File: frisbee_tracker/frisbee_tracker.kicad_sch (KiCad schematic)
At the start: 18 parts, among them IC1 NRF54L05-QFAA-R7, J1 UJC-H-G-SMT-2-P6-TR, U1 AP2210N-3.3TRG1, U2 BQ24072RGTT, U3 BMI323

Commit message: Rough draft of schematic complete
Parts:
- added AE1: RFANT3216120A5T, ANT_RFANT3216120A5T_WAL, symbol RFANT3216120A5T:RFANT3216120A5T
- added C10, C11, C8, C9: 0.1 uF Ceramic, symbol Device:C
- added C12: 2.2 nF Ceramic, symbol Device:C
- added C13, C14: 2.2 uF Ceramic, symbol Device:C
- added C15: 10 nF Ceramic, symbol Device:C
- added C16: 3.9 pF Ceramic, symbol Device:C
- added C17, C18: 100nF Ceramic, symbol Device:C
- added C19: 100 nF Ceramic, symbol Device:C
- added C20: GJM0335C1E1R5WB01, symbol Device:C
- added C21: GJM0335C1E2R0WB01, symbol Device:C
- added C22: 0.3 pF Ceramic, symbol Device:C
- added C7: 10 uF Ceramic, symbol Device:C
- added D1, D2, D3, D4: 5991090147F, symbol Device:LED
- added FB1: BLM18KG121TN1D, symbol Device:FerriteBead
- added J2: FTSH-105-01-L-DV-K, digikey-footprints:PinHeader_2x5_P1.27_SMD, symbol dk_Rectangular-Connectors-Headers-Male-Pins:FTSH-105-01-L-DV-K
- added L1: 4.7 uH, symbol Device:L
- added L2: LQP03HQ2N7B02, symbol Device:L
- added L3, L4: LQP03HQ3N5B02, symbol Device:L
- added R10, R7, R8: 4.7 kOhm, symbol Device:R_US
- added R11, R12, R13, R14: 68 Ohm, symbol Device:R_US
- added R15, R16: 10 kOhm, symbol Device:R_US
- added R17: 1 MOhm, symbol Device:R_US
- added R6: 1 kOhm, symbol Device:R_US
- added R9: 1.3 kOhm, symbol Device:R_US
- added U4, U5, U6, U7: BSS138, SOT-23_3L_ONS, symbol BSS138:BSS138
- added Y1: 32 MHz, symbol Device:Crystal
- added Y2: 32.768 kHz, symbol Device:Crystal
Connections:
- net GND: now also IC1.32 (VSS_PA), IC1.44 (VSS), IC1.49 (EP), U3.1 (SDO), U3.6 (GNDIO), U3.7 (GND), C10.1, C11.1, C12.1, C13.1, C14.1, C15.1, C16.1, C17.2, C18.1, C19.1, C20.1, C21.2, C22.1, C7.1, C8.1, C9.1, J2.3, J2.5, R10.2, R17.1, U4.2 (S), U5.2 (S), U6.2 (S), U7.2 (S)
- net at U2.14 (TMR): now also R17.2
- net at C3.1, H1.1, U2.2 (BAT)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: now also R9.2
- net at U2.7 (~{PGOOD}): now also IC1.18 (P2.07/TRACEDATA[0]/SWO/SPI.DCX), R16.1
- net at U2.9 (~{CHG}): now also IC1.17 (P2.06/TRACECLK/SPI.SCK), R15.1
- net at C6.1, U1.2 (VOUT): now also IC1.10 (VDD_1), IC1.22 (VDD_2), IC1.36 (VDD_3), IC1.47 (VDD_4), IC1.48 (VDD_5), U3.12 (CSB), U3.5 (VDDIO), U3.8 (VDD), C10.2, C11.2, C17.1, C18.2, C7.2, C8.2, C9.2, J2.1, R11.2, R12.2, R13.2, R14.2, R15.2, R16.2, R7.1, R8.1
- net at U3.13 (SCX): now also IC1.12 (P2.01/SPI.SCK), R8.2
- net at U3.14 (SDX): now also IC1.11 (P2.00/SPI.DCX), R7.2
- net at U3.4 (INT1): now also IC1.23 (P0.00)
- net at U3.9 (INT2): now also IC1.24 (P0.01)
- net at IC1.1 (P1.00/XL1): now also Y2.2
- net at IC1.13 (P2.02/SPI.SDI/SDO): now also U4.1 (G)
- net at IC1.14 (P2.03): now also U5.1 (G)
- net at IC1.15 (P2.04/SPI.SDI/SDO): now also U6.1 (G)
- net at IC1.16 (P2.05/SPI.CS): now also U7.1 (G)
- net at IC1.2 (P1.01/XL2): now also Y2.1
- net at IC1.25 (SWDIO): now also J2.2
- net at IC1.26 (SWDCLK): now also J2.4
- net at IC1.30 (NRESET): now also C16.2, R6.1
- net at IC1.31 (ANT): now also L2.1
- net at IC1.33 (DECRF): now also IC1.43 (DECA), C12.2, C13.2, C15.2, FB1.2
- net at IC1.34 (XC1): now also Y1.2
- net at IC1.35 (XC2): now also Y1.1
- net at IC1.45 (DECD): now also C14.2, FB1.1, L1.2
- net at IC1.46 (DCC): now also L1.1
- net at IC1.9 (P1.08/CLK16M/TAMPC): now also C19.2, R10.1, R9.1
- new net: D4.2 (A), R14.1
- new net: D2.1 (K), U5.3 (D)
- new net: D2.2 (A), R12.1
- new net: D3.2 (A), R13.1
- new net: D3.1 (K), U6.3 (D)
- new net: D1.1 (K), U4.3 (D)
- new net: D1.2 (A), R11.1
- new net: C20.2, L2.2, L3.1
- new net: C21.1, L3.2, L4.1
- new net: J2.6, R6.2
- new net: D4.1 (K), U7.3 (D)
- new net: AE1.1, C22.2, L4.2
- no-connect marks 1 -> 23
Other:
- note added: "C21 MUST ONLY CONNECT TO BOTTOM LAYER GROUND"
- note added: "C21:"
- note added: "C22:"
- note added: "CONNECT PIN 32 ONLY TO PIN 49 (CENTER PAD)"
- note added: "L2:"
- note added: "L3:"
- note added: "L4:"
- note added: "PUSH-PULL INTERRUPT CONFIG"
- moved on the sheet: H1, H2, U3

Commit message: start of PCB design
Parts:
- AE1: footprint ANT_RFANT3216120A5T_WAL -> footprints:RFANT3216120A5T
- C1, C10, C11, C12, C13, C14, C15, C16, C17, C18, C19, C2, C22, C3, C4, C5, C6, C7, C8, C9: footprint (none) -> Capacitor_SMD:C_0603_1608Metric
- C20, C21: footprint (none) -> Capacitor_SMD:C_0201_0603Metric
- D1, D2, D3, D4: footprint (none) -> LED_SMD:LED_0603_1608Metric
- FB1: footprint (none) -> footprints:BLM18KG121TN1D
- H1, H2: footprint (none) -> Connector_PinHeader_1.27mm:PinHeader_1x01_P1.27mm_Vertical
- IC1: footprint (none) -> footprints:NRF54L05-QFAA-R7
- J1: footprint (none) -> footprints:UJC-H-G-SMT-2-P6-TR
- J2: footprint digikey-footprints:PinHeader_2x5_P1.27_SMD -> footprints:FTSH-105-01-L-DV-K
- L1: footprint (none) -> Inductor_SMD:L_0603_1608Metric
- L2: footprint (none) -> footprints:LQP03HQ2N7B02D
- L3, L4: footprint (none) -> footprints:LQP03HQ3N5B02D
- R1, R10, R11, R12, R13, R14, R15, R16, R17, R2, R3, R4, R5, R6, R7, R8, R9: footprint (none) -> Resistor_SMD:R_0603_1608Metric
- U1: footprint (none) -> footprints:AP2210N-3.3TRG1
- U2: footprint (none) -> footprints:BQ24072RGTT
- U3: footprint (none) -> footprints:BMI323
- U4, U5, U6, U7: footprint SOT-23_3L_ONS -> footprints:BSS138
- Y1: footprint (none) -> footprints:ECS-320-8-37B2-JTY-TR
- Y2: footprint (none) -> footprints:Q 0,032768-JTX210-7-20-T1-HMR-70K-LF
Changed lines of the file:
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@@
 			)
 		)
-		(property "Footprint" ""
+		(property "Footprint" "footprints:Q 0,032768-JTX210-7-20-T1-HMR-70K-LF"
 			(at 38.1 88.9 0)
 			(effects
@@
 			)
 		)
-		(property "Footprint" ""
+		(property "Footprint" "Capacitor_SMD:C_0603_1608Metric"
 			(at 120.3452 35.56 0)
 			(effects
@@
 			)
 		)
-		(property "Footprint" ""
+		(property "Footprint" "Capacitor_SMD:C_0603_1608Metric"
 			(at 241.3 101.9048 0)
 			(effects
@@
 			)
 		)
-		(property "Footprint" ""
+		(property "Footprint" "Capacitor_SMD:C_0603_1608Metric"
 			(at 73.66 58.1152 0)
 			(effects
@@
 			)
 		)
-		(property "Footprint" ""
+		(property "Footprint" "Resistor_SMD:R_0603_1608Metric"
 			(at 20.066 176.784 90)
 			(effects
@@
 			)
 		)
-		(property "Footprint" ""
+		(property "Footprint" "LED_SMD:LED_0603_1608Metric"
 			(at 35.56 168.91 0)
 			(effects
@@
 			)
 		)
-		(property "Footprint" ""
+		(property "Footprint" "Resistor_SMD:R_0603_1608Metric"
 			(at 27.686 176.784 90)
 			(effects
@@
 			)
 		)
-		(property "Footprint" ""
+		(property "Footprint" "LED_SMD:LED_0603_1608Metric"
 			(at 26.67 168.91 0)
 			(effects
@@
 			)
 		)
-		(property "Footprint" ""
+		(property "Footprint" "Capacitor_SMD:C_0603_1608Metric"
 			(at 100.6348 46.99 0)
 			(effects
@@
 			)
 		)
-		(property "Footprint" ""
+		(property "Footprint" "Capacitor_SMD:C_0603_1608Metric"
 			(at 25.0952 116.84 0)
 			(effects
@@
 			)
 		)
-		(property "Footprint" ""
+		(property "Footprint" "footprints:BQ24072RGTT"
 			(at 228.6 73.66 0)
 			(effects
@@
 			)
 		)
-		(property "Footprint" ""
+		(property "Footprint" "Resistor_SMD:R_0603_1608Metric"
 			(at 181.356 45.974 90)
 			(effects
@@
 			)
 		)
-		(property "Footprint" "SOT-23_3L_ONS"
+		(property "Footprint" "footprints:BSS138"
 			(at -1.27 151.13 0)
 			(effects
@@
 			)
 		)
-		(property "Footprint" ""
+		(property "Footprint" "Capacitor_SMD:C_0603_1608Metric"
 			(at 261.62 57.4548 0)
 			(effects
@@
 			)
 		)
-		(property "Footprint" ""
+		(property "Footprint" "Resistor_SMD:R_0603_1608Metric"
 			(at 45.466 176.784 90)
 			(effects
@@
 			)
 		)
-		(property "Footprint" ""
+		(property "Footprint" "Resistor_SMD:R_0603_1608Metric"
 			(at 260.604 80.264 90)
 			(effects
@@
 			)
 		)
-		(property "Footprint" ""
+		(property "Footprint" "Capacitor_SMD:C_0603_1608Metric"
 			(at 265.43 72.6948 0)
 			(effects
@@
 			)
 		)
-		(property "Footprint" ""
+		(property "Footprint" "Capacitor_SMD:C_0603_1608Metric"
 			(at 125.73 48.5648 0)
 			(effects
@@
 			)
 		)
-		(property "Footprint" ""
+		(property "Footprint" "Resistor_SMD:R_0603_1608Metric"
 			(at 175.514 102.616 90)
 			(effects
@@
 			)
 		)
-		(property "Footprint" ""
+		(property "Footprint" "Resistor_SMD:R_0603_1608Metric"
 			(at 186.436 49.784 90)
 			(effects
@@
 			)
 		)
-		(property "Footprint" ""
+		(property "Footprint" "Capacitor_SMD:C_0603_1608Metric"
 			(at 266.7 20.6248 0)
 			(effects
@@
 			)
 		)
-		(property "Footprint" ""
+		(property "Footprint" "Connector_PinHeader_1.27mm:PinHeader_1x01_P1.27mm_Vertical"
 			(at 266.7 43.18 0)
 			(effects
@@
 			)
 		)
-		(property "Footprint" "SOT-23_3L_ONS"
+		(property "Footprint" "footprints:BSS138"
 			(at -1.27 179.07 0)
 			(effects
@@
 			)
 		)
-		(property "Footprint" ""
+		(property "Footprint" "footprints:LQP03HQ3N5B02D"
 			(at 154.94 93.98 0)
 			(effects
@@
 			)
 		)
-		(property "Footprint" ""
+		(property "Footprint" "Resistor_SMD:R_0603_1608Metric"
 			(at 167.894 102.616 90)
 			(effects
@@
 			)
 		)
-		(property "Footprint" ""
+		(property "Footprint" "footprints:BMI323"
 			(at 201.93 130.81 0)
 			(effects
@@
 			)
 		)
-		(property "Footprint" ""
+		(property "Footprint" "Resistor_SMD:R_0603_1608Metric"
 			(at 272.034 26.924 90)
 			(effects
@@
 			)
 		)
-		(property "Footprint" ""
+		(property "Footprint" "footprints:BLM18KG121TN1D"
 			(at 88.9 48.768 90)
 			(effects
@@
 			)
 		)
-		(property "Footprint" ""
+		(property "Footprint" "Resistor_SMD:R_0603_1608Metric"
 			(at 147.574 110.744 90)
 			(effects
@@
 			)
 		)
-		(property "Footprint" ""
+		(property "Footprint" "Capacitor_SMD:C_0603_1608Metric"
 			(at 130.5052 101.6 0)
 			(effects
@@
 			)
 		)
-		(property "Footprint" ""
+		(property "Footprint" "Capacitor_SMD:C_0603_1608Metric"
 			(at 64.77 57.4548 0)
 			(effects
@@
 			)
 		)
-		(property "Footprint" "SOT-23_3L_ONS"
+		(property "Footprint" "footprints:BSS138"
 			(at -1.27 193.04 0)
 			(effects
@@
 			)
 		)
-		(property "Footprint" ""
+		(property "Footprint" "Resistor_SMD:R_0603_1608Metric"
 			(at 139.446 32.004 90)
 			(effects
@@
 			)
 		)
-		(property "Footprint" ""
+		(property "Footprint" "Capacitor_SMD:C_0603_1608Metric"
 			(at 205.74 159.0548 0)
 			(effects
@@
 			)
 		)
-		(property "Footprint" "SOT-23_3L_ONS"
+		(property "Footprint" "footprints:BSS138"
 			(at -1.27 165.1 0)
 			(effects
@@
 			)
 		)
-		(property "Footprint" ""
+		(property "Footprint" "Resistor_SMD:R_0603_1608Metric"
 			(at 207.264 77.724 90)
 			(effects
@@
 			)
 		)
-		(property "Footprint" ""
+		(property "Footprint" "Capacitor_SMD:C_0603_1608Metric"
 			(at 64.77 48.5648 0)
 			(effects
@@
 			)
 		)
-		(property "Footprint" ""
+		(property "Footprint" "Capacitor_SMD:C_0603_1608Metric"
 			(at 87.63 194.0052 0)
 			(effects
@@
 			)
 		)
-		(property "Footprint" ""
+		(property "Footprint" "Capacitor_SMD:C_0201_0603Metric"
 			(at 147.32 91.1352 0)
 			(effects
@@
 			)
 		)
-		(property "Footprint" ""
+		(property "Footprint" "Resistor_SMD:R_0603_1608Metric"
 			(at 250.444 62.484 90)
 			(effects
@@
 			)
 		)
-		(property "Footprint" ""
+		(property "Footprint" "Capacitor_SMD:C_0603_1608Metric"
 			(at 154.94 81.5848 0)
 			(effects
@@
 			)
 		)
-		(property "Footprint" ""
+		(property "Footprint" "footprints:UJC-H-G-SMT-2-P6-TR"
 			(at 182.88 29.21 0)
 			(effects
@@
 			)
 		)
-		(property "Footprint" ""
+		(property "Footprint" "Capacitor_SMD:C_0603_1608Metric"
 			(at 140.6652 101.6 0)
 			(effects
@@
 			)
 		)
-		(property "Footprint" "ANT_RFANT3216120A5T_WAL"
+		(property "Footprint" "footprints:RFANT3216120A5T"
 			(at 142.24 73.66 0)
 			(effects
@@
 			)
 		)
-		(property "Footprint" ""
+		(property "Footprint" "footprints:ECS-320-8-37B2-JTY-TR"
 			(at 116.84 93.98 0)
 			(effects
@@
 			)
 		)
-		(property "Footprint" ""
+		(property "Footprint" "LED_SMD:LED_0603_1608Metric"
 			(at 44.45 168.91 0)
 			(effects
@@
 			)
 		)
-		(property "Footprint" ""
+		(property "Footprint" "Capacitor_SMD:C_0201_0603Metric"
 			(at 147.6248 99.06 0)
 			(effects
@@
 			)
 		)
-		(property "Footprint" ""
+		(property "Footprint" "footprints:LQP03HQ3N5B02D"
 			(at 154.94 86.36 0)
 			(effects
@@
 			)
 		)
-		(property "Footprint" ""
+		(property "Footprint" "LED_SMD:LED_0603_1608Metric"
 			(at 19.05 168.91 0)
 			(effects
@@
 			)
 		)
-		(property "Footprint" ""
+		(property "Footprint" "footprints:NRF54L05-QFAA-R7"
 			(at 106.68 173.66 0)
 			(effects
@@
 			)
 		)
-		(property "Footprint" ""
+		(property "Footprint" "Capacitor_SMD:C_0603_1608Metric"
 			(at 104.14 16.8148 0)
 			(effects
@@
 			)
 		)
-		(property "Footprint" ""
+		(property "Footprint" "Capacitor_SMD:C_0603_1608Metric"
 			(at 111.76 68.8848 0)
 			(effects
@@
 			)
 		)
-		(property "Footprint" ""
+		(property "Footprint" "Resistor_SMD:R_0603_1608Metric"
 			(at 36.576 176.784 90)
 			(effects
@@
 			)
 		)
-		(property "Footprint" ""
+		(property "Footprint" "footprints:LQP03HQ2N7B02D"
 			(at 154.94 101.6 0)
 			(effects
@@
 			)
 		)
-		(property "Footprint" ""
+		(property "Footprint" "Resistor_SMD:R_0603_1608Metric"
 			(at 170.434 153.416 90)
 			(effects
@@
 			)
 		)
-		(property "Footprint" ""
+		(property "Footprint" "Capacitor_SMD:C_0603_1608Metric"
 			(at 241.3 159.0548 0)
 			(effects
@@
 			)
 		)
-		(property "Footprint" ""
+		(property "Footprint" "Inductor_SMD:L_0603_1608Metric"
 			(at 76.2 46.99 0)
 			(effects
@@
 			)
 		)
-		(property "Footprint" "digikey-footprints:PinHeader_2x5_P1.27_SMD"
+		(property "Footprint" "footprints:FTSH-105-01-L-DV-K"
 			(at 152.4 58.42 0)
 			(effects
@@
 			)
 		)
-		(property "Footprint" ""
+		(property "Footprint" "Connector_PinHeader_1.27mm:PinHeader_1x01_P1.27mm_Vertical"
 			(at 279.4 43.18 0)
 			(effects
@@
 			)
 		)
-		(property "Footprint" ""
+		(property "Footprint" "Resistor_SMD:R_0603_1608Metric"
 			(at 180.594 153.416 90)
 			(effects
@@
 			)
 		)
-		(property "Footprint" ""
+		(property "Footprint" "Resistor_SMD:R_0603_1608Metric"
 			(at 267.716 34.544 90)
 			(effects
@@
 			)
 		)
-		(property "Footprint" ""
+		(property "Footprint" "footprints:AP2210N-3.3TRG1"
 			(at 71.12 29.21 0)
 			(effects
@@
 			)
 		)
-		(property "Footprint" ""
+		(property "Footprint" "Capacitor_SMD:C_0603_1608Metric"
 			(at 136.1948 111.76 0)
 			(effects

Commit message: PCB design 90% complete
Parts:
- removed J2: FTSH-105-01-L-DV-K, footprints:FTSH-105-01-L-DV-K, symbol dk_Rectangular-Connectors-Headers-Male-Pins:FTSH-105-01-L-DV-K
- added J2: FTSH-103-01-L-D, footprints:FTSH-103-01-L-D, symbol FTSH-103-01-L-D:FTSH-103-01-L-D
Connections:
- net GND: now also J2.03, J2.05
- net at C10.2, C11.2, C17.1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: now also J2.01
- net at IC1.18 (P2.07/TRACEDATA[0]/SWO/SPI.DCX), R16.1: now also U2.9 (~{CHG}); no longer U2.7 (~{PGOOD})
- net at IC1.17 (P2.06/TRACECLK/SPI.SCK), R15.1: now also U2.7 (~{PGOOD}); no longer U2.9 (~{CHG})
- net at R6.2: now also J2.06
- net at IC1.25 (SWDIO): now also J2.02
- net at IC1.26 (SWDCLK): now also J2.04
- no-connect marks 23 -> 19

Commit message: Rough draft of PCB completed
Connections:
- net at C1.2, J1.SH1 (SHIELD), J1.SH2 (SHIELD__1)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: no longer J1.SH3 (SHIELD__2), J1.SH4 (SHIELD__3)
- no-connect marks 19 -> 21
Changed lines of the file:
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@@
+	)
+	(junction
+		(at 165.1 43.18)
+		(diameter 0)
+		(color 0 0 0 0)
 	)
 	(junction
@@
 	)
 	(junction
-		(at 162.56 41.91)
-		(diameter 0)
-		(color 0 0 0 0)
-	)
-	(junction
 		(at 111.76 49.53)
 		(diameter 0)
@@
 	)
 	(junction
+		(at 138.43 43.18)
+		(diameter 0)
+		(color 0 0 0 0)
+	)
+	(junction
 		(at 111.76 40.64)
 		(diameter 0)
@@
 	)
 	(junction
-		(at 138.43 41.91)
-		(diameter 0)
-		(color 0 0 0 0)
-	)
-	(junction
 		(at 181.61 160.02)
 		(diameter 0)
@@
 	)
 	(junction
-		(at 160.02 41.91)
-		(diameter 0)
-		(color 0 0 0 0)
-	)
-	(junction
 		(at 44.45 193.04)
 		(diameter 0)
@@
 	(junction
 		(at 266.7 27.94)
-		(diameter 0)
-		(color 0 0 0 0)
-	)
-	(junction
-		(at 165.1 41.91)
 		(diameter 0)
 		(color 0 0 0 0)
@@
 	)
 	(no_connect
+		(at 160.02 41.91)
+	)
+	(no_connect
 		(at 44.45 109.22)
 	)
@@
 	)
 	(no_connect
+		(at 162.56 41.91)
+	)
+	(no_connect
 		(at 44.45 111.76)
 	)
@@
 	(wire
 		(pts
+			(xy 167.64 43.18) (xy 167.64 41.91)
+		)
+		(stroke
+			(width 0)
+			(type default)
+		)
+	)
+	(wire
+		(pts
 			(xy 67.31 172.72) (xy 67.31 201.93)
 		)
@@
 	(wire
 		(pts
-			(xy 165.1 41.91) (xy 167.64 41.91)
+			(xy 165.1 43.18) (xy 167.64 43.18)
 		)
 		(stroke
@@
 	(wire
 		(pts
-			(xy 119.38 35.56) (xy 119.38 41.91)
+			(xy 119.38 35.56) (xy 119.38 43.18)
 		)
 		(stroke
@@
 	(wire
 		(pts
-			(xy 119.38 41.91) (xy 138.43 41.91)
+			(xy 119.38 43.18) (xy 138.43 43.18)
 		)
 		(stroke
@@
 	(wire
 		(pts
-			(xy 160.02 41.91) (xy 162.56 41.91)
-		)
-		(stroke
-			(width 0)
-			(type default)
-		)
-	)
-	(wire
-		(pts
 			(xy 246.38 133.35) (xy 242.57 133.35)
 		)
@@
 	(wire
 		(pts
+			(xy 165.1 41.91) (xy 165.1 43.18)
+		)
+		(stroke
+			(width 0)
+			(type default)
+		)
+	)
+	(wire
+		(pts
 			(xy 120.65 101.6) (xy 120.65 93.98)
 		)
@@
 	(wire
 		(pts
-			(xy 138.43 41.91) (xy 138.43 35.56)
-		)
-		(stroke
-			(width 0)
-			(type default)
-		)
-	)
-	(wire
-		(pts
 			(xy 246.38 17.78) (xy 111.76 17.78)
 		)
@@
 	(wire
 		(pts
-			(xy 162.56 41.91) (xy 165.1 41.91)
-		)
-		(stroke
-			(width 0)
-			(type default)
-		)
-	)
-	(wire
-		(pts
 			(xy 246.38 115.57) (xy 246.38 133.35)
 		)
@@
 	(wire
 		(pts
+			(xy 165.1 43.18) (xy 138.43 43.18)
+		)
+		(stroke
+			(width 0)
+			(type default)
+		)
+	)
+	(wire
+		(pts
 			(xy 69.85 204.47) (xy 69.85 172.72)
 		)
@@
 	(wire
 		(pts
+			(xy 138.43 35.56) (xy 138.43 43.18)
+		)
+		(stroke
+			(width 0)
+			(type default)
+		)
+	)
+	(wire
+		(pts
 			(xy 111.76 44.45) (xy 111.76 49.53)
 		)
@@
 		)
 		(stroke
-			(width 0)
-			(type default)
-		)
-	)
-	(wire
-		(pts
-			(xy 138.43 41.91) (xy 160.02 41.91)
-		)
-		(stroke

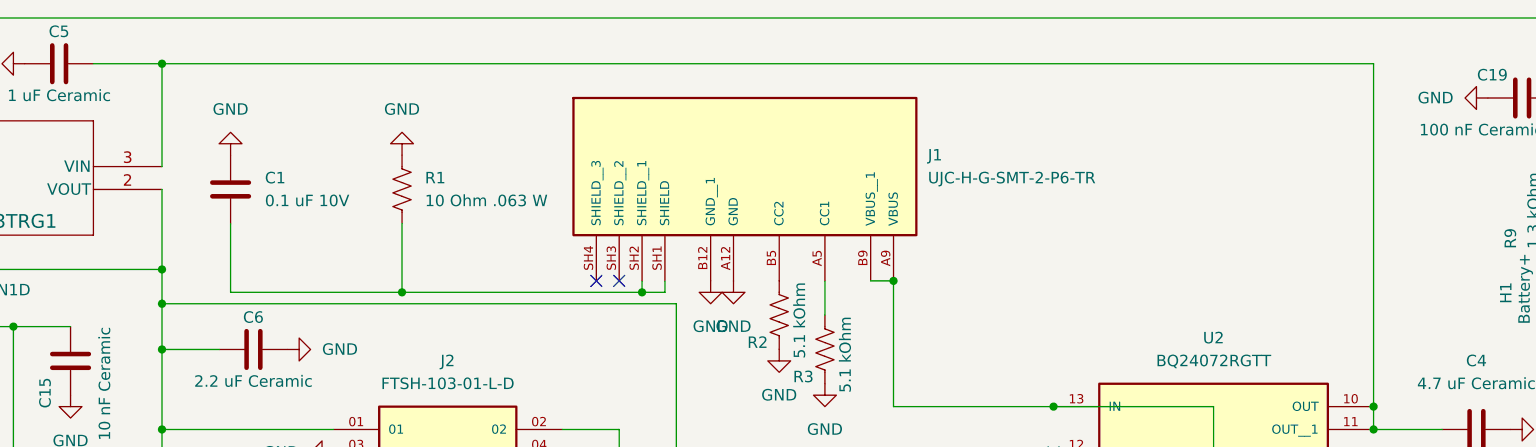
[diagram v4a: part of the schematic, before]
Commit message: Added switch and Shottky diode to schematic
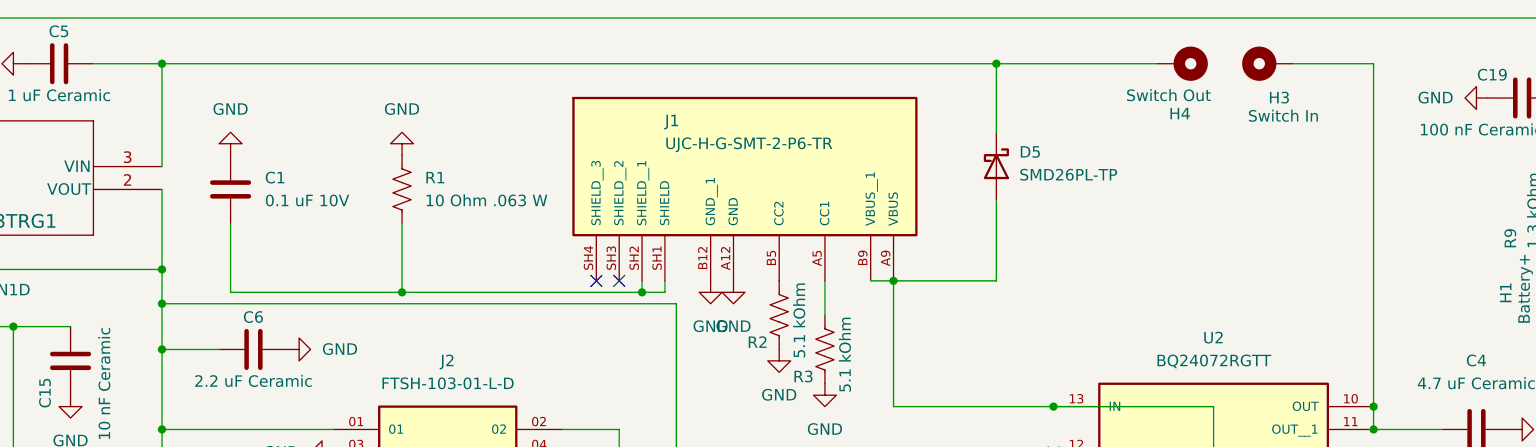
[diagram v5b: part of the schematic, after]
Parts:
- added D5: SMD26PL-TP, footprints:SMD26PL-TP, symbol Device:D_Schottky
- added H3: Switch In, Connector_PinHeader_1.27mm:PinHeader_1x01_P1.27mm_Vertical, symbol Mechanical:MountingHole_Pad
- added H4: Switch Out, Connector_PinHeader_1.27mm:PinHeader_1x01_P1.27mm_Vertical, symbol Mechanical:MountingHole_Pad
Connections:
- net at C2.1, J1.A9 (VBUS), J1.B9 (VBUS__1)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: now also D5.2 (A)
- net at C4.1, U2.10 (OUT), U2.11 (OUT__1): now also H3.1; no longer C5.2, U1.3 (VIN)
- new net: C5.2, D5.1 (K), H4.1, U1.3 (VIN)
